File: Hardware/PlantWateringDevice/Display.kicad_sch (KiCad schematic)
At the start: 14 parts, among them SW1 SW_Push, U7 SC39-11EWA

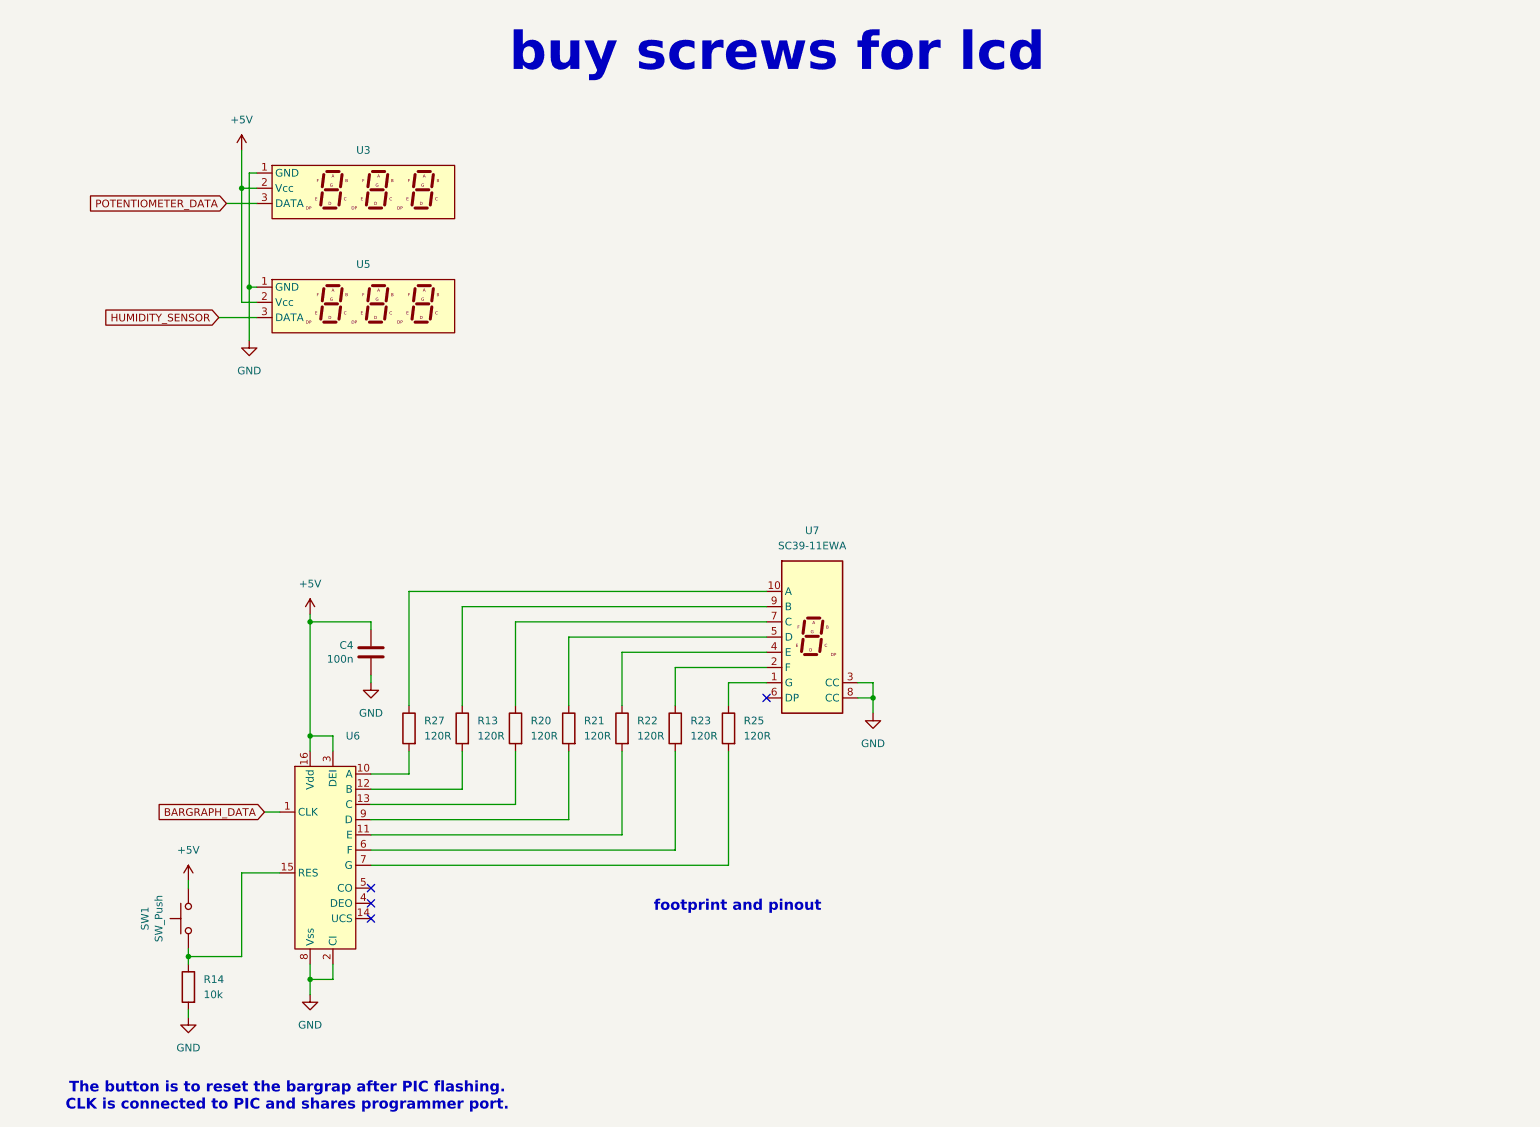
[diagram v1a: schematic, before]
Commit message: hierarchical block diagram structure in kicad
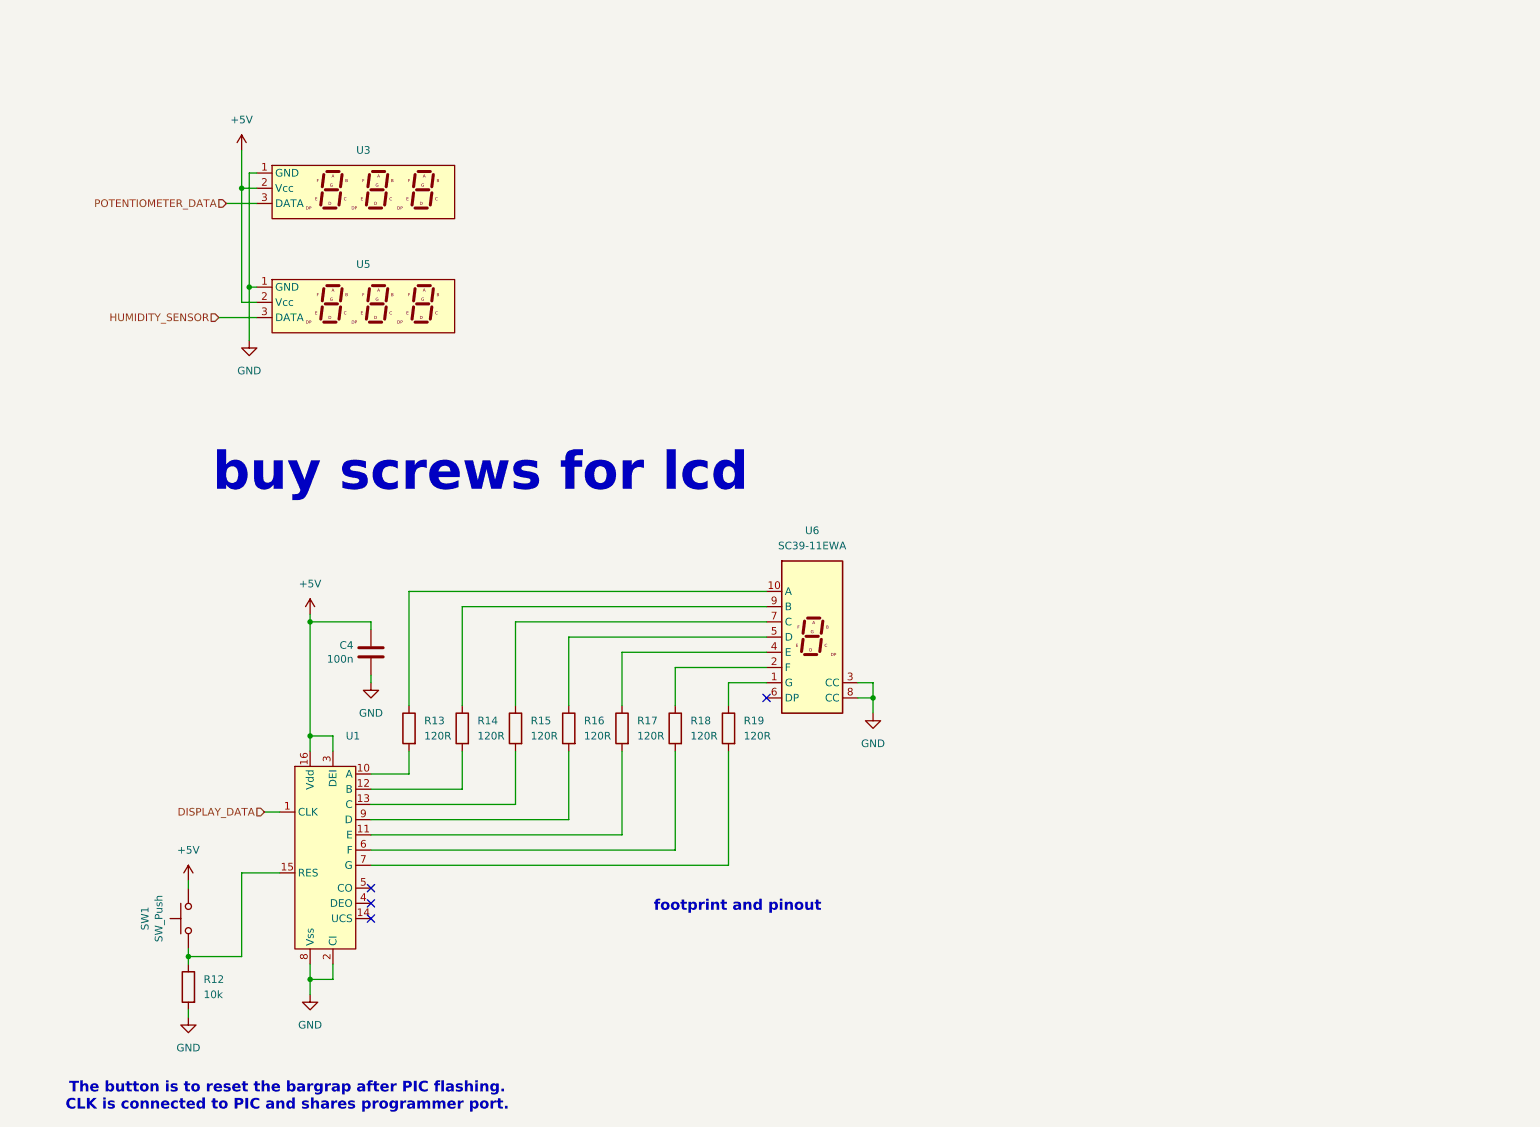
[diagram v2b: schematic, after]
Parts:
- renumbered R14 to R12, R27 to R13, R13 to R14, R20 to R15, R21 to R16, R22 to R17, R23 to R18, R25 to R19, U6 to U1, U7 to U6
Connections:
- net BARGRAPH_DATA renamed DISPLAY_DATA
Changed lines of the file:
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@@
 (kicad_sch
-	(version 20260101)
+	(version 20260306)
 	(generator "eeschema")
 	(generator_version "10.0")
@@
 	(text "buy screws for lcd"
 		(exclude_from_sim no)
-		(at 144.018 15.494 0)
+		(at 94.488 85.598 0)
 		(effects
 			(font
@@
 		)
 	)
-	(global_label "POTENTIOMETER_DATA"
+	(hierarchical_label "HUMIDITY_SENSOR"
 		(shape input)
-		(at 52.07 40.64 180)
-		(fields_autoplaced yes)
+		(at 50.8 59.69 180)
 		(effects
 			(font
@@
 			(justify right)
 		)
-		(property "Intersheetrefs" "${INTERSHEET_REFS}"
-			(at 28.7649 40.64 0)
-			(hide yes)
-			(show_name no)
-			(do_not_autoplace no)
-			(effects
-				(font
-					(size 1.27 1.27)
-				)
-				(justify right)
-			)
-		)
-	)
-	(global_label "BARGRAPH_DATA"
+	)
+	(hierarchical_label "POTENTIOMETER_DATA"
 		(shape input)
-		(at 58.42 142.24 180)
-		(fields_autoplaced yes)
+		(at 52.07 40.64 180)
 		(effects
 			(font
@@
 			(justify right)
 		)
-		(property "Intersheetrefs" "${INTERSHEET_REFS}"
-			(at 40.1947 142.24 0)
-			(hide yes)
-			(show_name no)
-			(do_not_autoplace no)
-			(effects
-				(font
-					(size 1.27 1.27)
-				)
-				(justify right)
-			)
-		)
-	)
-	(global_label "HUMIDITY_SENSOR"
+	)
+	(hierarchical_label "DISPLAY_DATA"
 		(shape input)
-		(at 50.8 59.69 180)
-		(fields_autoplaced yes)
+		(at 58.42 142.24 180)
 		(effects
 			(font
@@
 			)
 			(justify right)
-		)
-		(property "Intersheetrefs" "${INTERSHEET_REFS}"
-			(at 30.7 59.69 0)
-			(hide yes)
-			(show_name no)
-			(do_not_autoplace no)
-			(effects
-				(font
-					(size 1.27 1.27)
-				)
-				(justify right)
-			)
 		)
 	)
@@
 		(instances
 			(project "PlantWateringDevice"
-				(path "/1ef241b3-83d7-48ae-bcca-b7d0eea44e63/d76ecc7e-66e3-47dc-9ce8-30fb2403ed3e"
+				(path "/1ef241b3-83d7-48ae-bcca-b7d0eea44e63/677803a8-5f3c-4ac5-8902-74d58e2a1af0"
 					(reference "C4")
 					(unit 1)
@@
 		(instances
 			(project "PlantWateringDevice"
-				(path "/1ef241b3-83d7-48ae-bcca-b7d0eea44e63/d76ecc7e-66e3-47dc-9ce8-30fb2403ed3e"
+				(path "/1ef241b3-83d7-48ae-bcca-b7d0eea44e63/677803a8-5f3c-4ac5-8902-74d58e2a1af0"
 					(reference "#PWR037")
 					(unit 1)
@@
 		(dnp no)
 		(fields_autoplaced yes)
-		(property "Reference" "R13"
+		(property "Reference" "R14"
 			(at 93.98 126.9999 0)
 			(show_name no)
@@
 		(instances
 			(project "PlantWateringDevice"
-				(path "/1ef241b3-83d7-48ae-bcca-b7d0eea44e63/d76ecc7e-66e3-47dc-9ce8-30fb2403ed3e"
-					(reference "R13")
+				(path "/1ef241b3-83d7-48ae-bcca-b7d0eea44e63/677803a8-5f3c-4ac5-8902-74d58e2a1af0"
+					(reference "R14")
 					(unit 1)
 				)
@@
 		(dnp no)
 		(fields_autoplaced yes)
-		(property "Reference" "U7"
+		(property "Reference" "U6"
 			(at 149.86 95.25 0)
 			(show_name no)
@@
 		)
 		(instances
-			(project ""
-				(path "/1ef241b3-83d7-48ae-bcca-b7d0eea44e63/d76ecc7e-66e3-47dc-9ce8-30fb2403ed3e"
-					(reference "U7")
+			(project "PlantWateringDevice"
+				(path "/1ef241b3-83d7-48ae-bcca-b7d0eea44e63/677803a8-5f3c-4ac5-8902-74d58e2a1af0"
+					(reference "U6")
 					(unit 1)
 				)
@@
 		(dnp no)
 		(fields_autoplaced yes)
-		(property "Reference" "U6"
+		(property "Reference" "U1"
 			(at 71.9933 129.54 0)
 			(show_name no)
@@
 		)
 		(instances
-			(project ""
-				(path "/1ef241b3-83d7-48ae-bcca-b7d0eea44e63/d76ecc7e-66e3-47dc-9ce8-30fb2403ed3e"
-					(reference "U6")
+			(project "PlantWateringDevice"
+				(path "/1ef241b3-83d7-48ae-bcca-b7d0eea44e63/677803a8-5f3c-4ac5-8902-74d58e2a1af0"
+					(reference "U1")
 					(unit 1)
 				)
@@
 		)
 		(instances
-			(project ""
-				(path "/1ef241b3-83d7-48ae-bcca-b7d0eea44e63/d76ecc7e-66e3-47dc-9ce8-30fb2403ed3e"
+			(project "PlantWateringDevice"
+				(path "/1ef241b3-83d7-48ae-bcca-b7d0eea44e63/677803a8-5f3c-4ac5-8902-74d58e2a1af0"
 					(reference "U3")
 					(unit 1)
@@
 		(dnp no)
 		(fields_autoplaced yes)
-		(property "Reference" "R27"
+		(property "Reference" "R13"
 			(at 85.09 126.9999 0)
 			(show_name no)
@@
 		(instances
 			(project "PlantWateringDevice"
-				(path "/1ef241b3-83d7-48ae-bcca-b7d0eea44e63/d76ecc7e-66e3-47dc-9ce8-30fb2403ed3e"
-					(reference "R27")
+				(path "/1ef241b3-83d7-48ae-bcca-b7d0eea44e63/677803a8-5f3c-4ac5-8902-74d58e2a1af0"
+					(reference "R13")
 					(unit 1)
 				)
@@
 		(instances
 			(project "PlantWateringDevice"
-				(path "/1ef241b3-83d7-48ae-bcca-b7d0eea44e63/d76ecc7e-66e3-47dc-9ce8-30fb2403ed3e"
+				(path "/1ef241b3-83d7-48ae-bcca-b7d0eea44e63/677803a8-5f3c-4ac5-8902-74d58e2a1af0"
 					(reference "#PWR039")
 					(unit 1)
@@
 		(dnp no)
 		(fields_autoplaced yes)
-		(property "Reference" "R20"
+		(property "Reference" "R15"
 			(at 102.87 126.9999 0)
 			(show_name no)
@@
 		(instances
 			(project "PlantWateringDevice"
-				(path "/1ef241b3-83d7-48ae-bcca-b7d0eea44e63/d76ecc7e-66e3-47dc-9ce8-30fb2403ed3e"
-					(reference "R20")
+				(path "/1ef241b3-83d7-48ae-bcca-b7d0eea44e63/677803a8-5f3c-4ac5-8902-74d58e2a1af0"
+					(reference "R15")
 					(unit 1)
 				)
@@
 		(instances
 			(project "PlantWateringDevice"
-				(path "/1ef241b3-83d7-48ae-bcca-b7d0eea44e63/d76ecc7e-66e3-47dc-9ce8-30fb2403ed3e"
+				(path "/1ef241b3-83d7-48ae-bcca-b7d0eea44e63/677803a8-5f3c-4ac5-8902-74d58e2a1af0"
 					(reference "#PWR042")
 					(unit 1)
@@
 		(instances
 			(project "PlantWateringDevice"
-				(path "/1ef241b3-83d7-48ae-bcca-b7d0eea44e63/d76ecc7e-66e3-47dc-9ce8-30fb2403ed3e"
+				(path "/1ef241b3-83d7-48ae-bcca-b7d0eea44e63/677803a8-5f3c-4ac5-8902-74d58e2a1af0"
 					(reference "#PWR040")
 					(unit 1)
@@
 		(instances
 			(project "PlantWateringDevice"
-				(path "/1ef241b3-83d7-48ae-bcca-b7d0eea44e63/d76ecc7e-66e3-47dc-9ce8-30fb2403ed3e"
+				(path "/1ef241b3-83d7-48ae-bcca-b7d0eea44e63/677803a8-5f3c-4ac5-8902-74d58e2a1af0"
 					(reference "U5")
 					(unit 1)
@@
 		(instances
 			(project "PlantWateringDevice"
-				(path "/1ef241b3-83d7-48ae-bcca-b7d0eea44e63/d76ecc7e-66e3-47dc-9ce8-30fb2403ed3e"
+				(path "/1ef241b3-83d7-48ae-bcca-b7d0eea44e63/677803a8-5f3c-4ac5-8902-74d58e2a1af0"
 					(reference "#PWR014")
 					(unit 1)
@@
 		(dnp no)
 		(fields_autoplaced yes)
-		(property "Reference" "R23"
+		(property "Reference" "R18"
 			(at 129.54 126.9999 0)
 			(show_name no)
@@
 		(instances
 			(project "PlantWateringDevice"
-				(path "/1ef241b3-83d7-48ae-bcca-b7d0eea44e63/d76ecc7e-66e3-47dc-9ce8-30fb2403ed3e"
-					(reference "R23")
+				(path "/1ef241b3-83d7-48ae-bcca-b7d0eea44e63/677803a8-5f3c-4ac5-8902-74d58e2a1af0"
+					(reference "R18")
 					(unit 1)
 				)
@@
 		(dnp no)
 		(fields_autoplaced yes)
-		(property "Reference" "R25"
+		(property "Reference" "R19"
 			(at 138.43 126.9999 0)
 			(show_name no)
@@
 		(instances
 			(project "PlantWateringDevice"
-				(path "/1ef241b3-83d7-48ae-bcca-b7d0eea44e63/d76ecc7e-66e3-47dc-9ce8-30fb2403ed3e"
-					(reference "R25")
+				(path "/1ef241b3-83d7-48ae-bcca-b7d0eea44e63/677803a8-5f3c-4ac5-8902-74d58e2a1af0"
+					(reference "R19")
 					(unit 1)
 				)
@@
 		(dnp no)
 		(fields_autoplaced yes)
-		(property "Reference" "R21"
+		(property "Reference" "R16"
 			(at 111.76 126.9999 0)
 			(show_name no)
@@
 		(instances
 			(project "PlantWateringDevice"
-				(path "/1ef241b3-83d7-48ae-bcca-b7d0eea44e63/d76ecc7e-66e3-47dc-9ce8-30fb2403ed3e"
-					(reference "R21")
+				(path "/1ef241b3-83d7-48ae-bcca-b7d0eea44e63/677803a8-5f3c-4ac5-8902-74d58e2a1af0"
+					(reference "R16")
 					(unit 1)
 				)
@@
 		)
 		(instances
-			(project ""
-				(path "/1ef241b3-83d7-48ae-bcca-b7d0eea44e63/d76ecc7e-66e3-47dc-9ce8-30fb2403ed3e"
+			(project "PlantWateringDevice"
+				(path "/1ef241b3-83d7-48ae-bcca-b7d0eea44e63/677803a8-5f3c-4ac5-8902-74d58e2a1af0"
 					(reference "#PWR019")
 					(unit 1)
@@
 		(instances
 			(project "PlantWateringDevice"
-				(path "/1ef241b3-83d7-48ae-bcca-b7d0eea44e63/d76ecc7e-66e3-47dc-9ce8-30fb2403ed3e"
+				(path "/1ef241b3-83d7-48ae-bcca-b7d0eea44e63/677803a8-5f3c-4ac5-8902-74d58e2a1af0"
 					(reference "#PWR09")
 					(unit 1)
@@
 		(dnp no)
 		(fields_autoplaced yes)
-		(property "Reference" "R14"
+		(property "Reference" "R12"
 			(at 48.26 170.1799 0)
 			(show_name no)
@@
 		(instances
 			(project "PlantWateringDevice"
-				(path "/1ef241b3-83d7-48ae-bcca-b7d0eea44e63/d76ecc7e-66e3-47dc-9ce8-30fb2403ed3e"
-					(reference "R14")
+				(path "/1ef241b3-83d7-48ae-bcca-b7d0eea44e63/677803a8-5f3c-4ac5-8902-74d58e2a1af0"
+					(reference "R12")
 					(unit 1)
 				)
@@
 		(instances
 			(project "PlantWateringDevice"
-				(path "/1ef241b3-83d7-48ae-bcca-b7d0eea44e63/d76ecc7e-66e3-47dc-9ce8-30fb2403ed3e"
+				(path "/1ef241b3-83d7-48ae-bcca-b7d0eea44e63/677803a8-5f3c-4ac5-8902-74d58e2a1af0"
 					(reference "#PWR032")
 					(unit 1)
@@
 		(instances
 			(project "PlantWateringDevice"
-				(path "/1ef241b3-83d7-48ae-bcca-b7d0eea44e63/d76ecc7e-66e3-47dc-9ce8-30fb2403ed3e"
+				(path "/1ef241b3-83d7-48ae-bcca-b7d0eea44e63/677803a8-5f3c-4ac5-8902-74d58e2a1af0"
 					(reference "SW1")
 					(unit 1)
@@
 		(dnp no)
 		(fields_autoplaced yes)
-		(property "Reference" "R22"
+		(property "Reference" "R17"
 			(at 120.65 126.9999 0)
 			(show_name no)
@@
 		(instances
 			(project "PlantWateringDevice"
-				(path "/1ef241b3-83d7-48ae-bcca-b7d0eea44e63/d76ecc7e-66e3-47dc-9ce8-30fb2403ed3e"
-					(reference "R22")
+				(path "/1ef241b3-83d7-48ae-bcca-b7d0eea44e63/677803a8-5f3c-4ac5-8902-74d58e2a1af0"
+					(reference "R17")
 					(unit 1)
 				)
